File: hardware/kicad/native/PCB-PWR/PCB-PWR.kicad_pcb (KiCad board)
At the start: 4 copper layers, 90 x 60 mm, 66 parts, among them J1 43045-0213, J2 43045-1202, Q1 CSD18540Q5B, U1 LM74700QDBVRQ1, U2 INA226AIDGSR, U3 LMR604403SRAKR, U4 LMR604403SRAKR, U5 TPS7A2018PDBVR

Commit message: pcb-pwr: apply bootstrap routing candidate
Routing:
- net BOOT_3V8: track 0.00 -> 1.28 mm
- net BOOT_3V3: track 0.00 -> 1.28 mm
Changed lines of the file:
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@@
 		(layer "Edge.Cuts")
+	)
+	(segment
+		(start 54.925 15.125)
+		(end 55.055 16.4)
+		(width 0.5)
+		(layer "F.Cu")
+		(net 5)
+	)
+	(segment
+		(start 54.925 43.125)
+		(end 55.055 44.4)
+		(width 0.5)
+		(layer "F.Cu")
+		(net 4)
 	)
 	(embedded_fonts no)

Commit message: pcb-pwr: apply LM74700 VCAP routing candidate
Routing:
- net LM74700_VCAP: track 0.00 -> 3.16 mm
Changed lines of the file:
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@@
 		(net 4)
+	)
+	(segment
+		(start 18.7 29.05)
+		(end 19.52 26)
+		(width 0.5)
+		(layer "F.Cu")
+		(net 16)
 	)
 	(embedded_fonts no)

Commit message: pcb-pwr: apply VBAT_RAW routing candidate
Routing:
- net VBAT_RAW: track 0.00 -> 2.90 mm
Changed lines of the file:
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@@
 		(net 16)
+	)
+	(segment
+		(start 7.7 31.25)
+		(end 10.6 31.25)
+		(width 4)
+		(layer "F.Cu")
+		(net 30)
 	)
 	(embedded_fonts no)

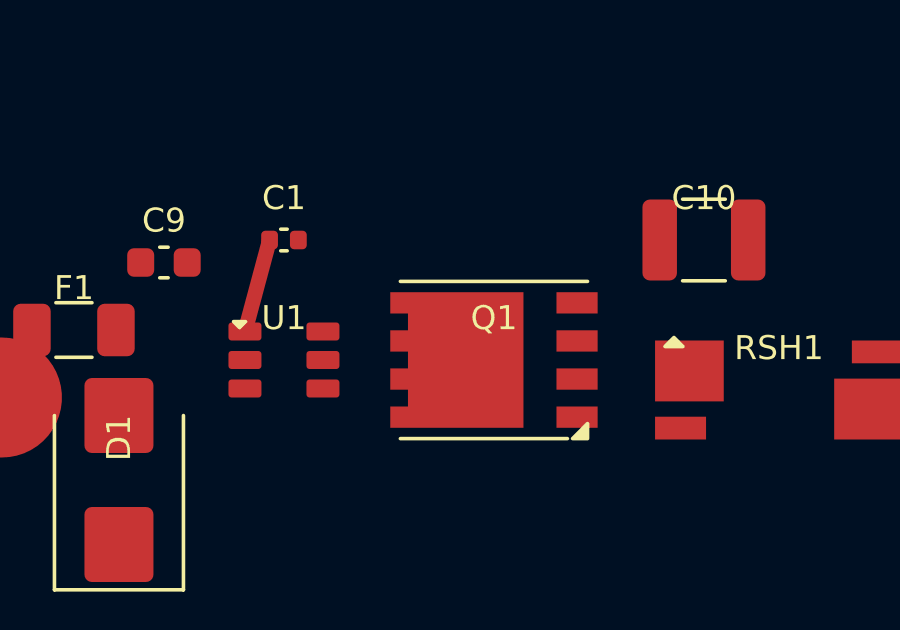
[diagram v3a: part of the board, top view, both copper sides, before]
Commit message: pcb-pwr: apply accepted REV_GATE route
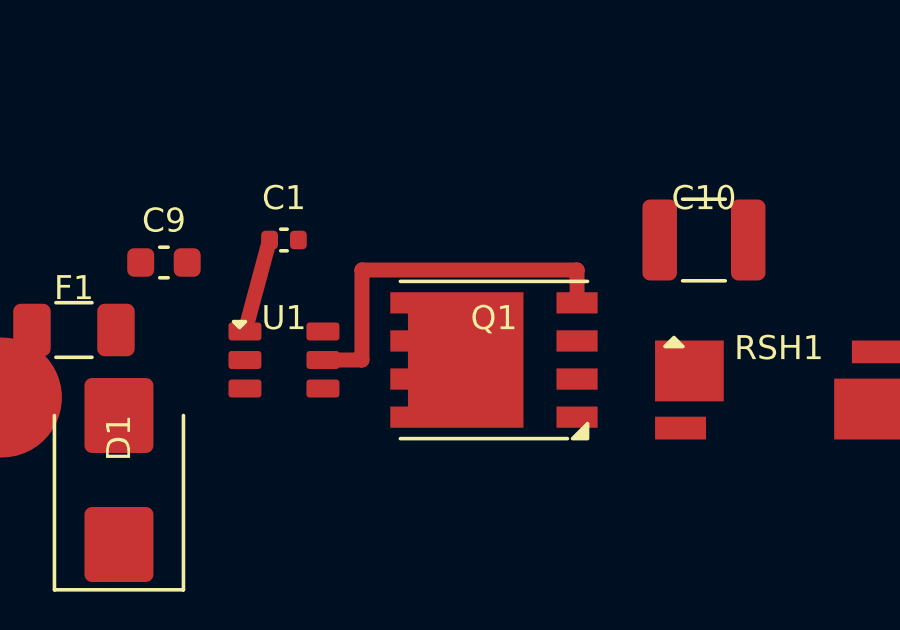
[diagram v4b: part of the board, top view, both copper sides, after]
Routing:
- net REV_GATE: track 0.00 -> 12.6 mm
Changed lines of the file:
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@@
 		(net 30)
+	)
+	(segment
+		(start 21.3 30)
+		(end 22.6 30)
+		(width 0.5)
+		(layer "F.Cu")
+		(net 21)
+	)
+	(segment
+		(start 22.6 30)
+		(end 22.6 27)
+		(width 0.5)
+		(layer "F.Cu")
+		(net 21)
+	)
+	(segment
+		(start 22.6 27)
+		(end 29.77 27)
+		(width 0.5)
+		(layer "F.Cu")
+		(net 21)
+	)
+	(segment
+		(start 29.77 27)
+		(end 29.77 28.095)
+		(width 0.5)
+		(layer "F.Cu")
+		(net 21)
 	)
 	(embedded_fonts no)

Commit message: hardware: apply PCB-PWR power-stage ECO-002
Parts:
- moved C4 4.00 mm to (57.8, 14.0), turned to 270 degrees
- moved C6 4.00 mm to (57.8, 42.0), turned to 270 degrees
- moved L1 1.75 mm to (62.5, 14.0)
- moved L2 1.75 mm to (62.5, 42.0)
- turned U3 to 90 degrees
- turned U4 to 90 degrees
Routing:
- net SW_3V8: track 0.00 -> 2.65 mm
- net SW_3V3: track 0.00 -> 2.65 mm

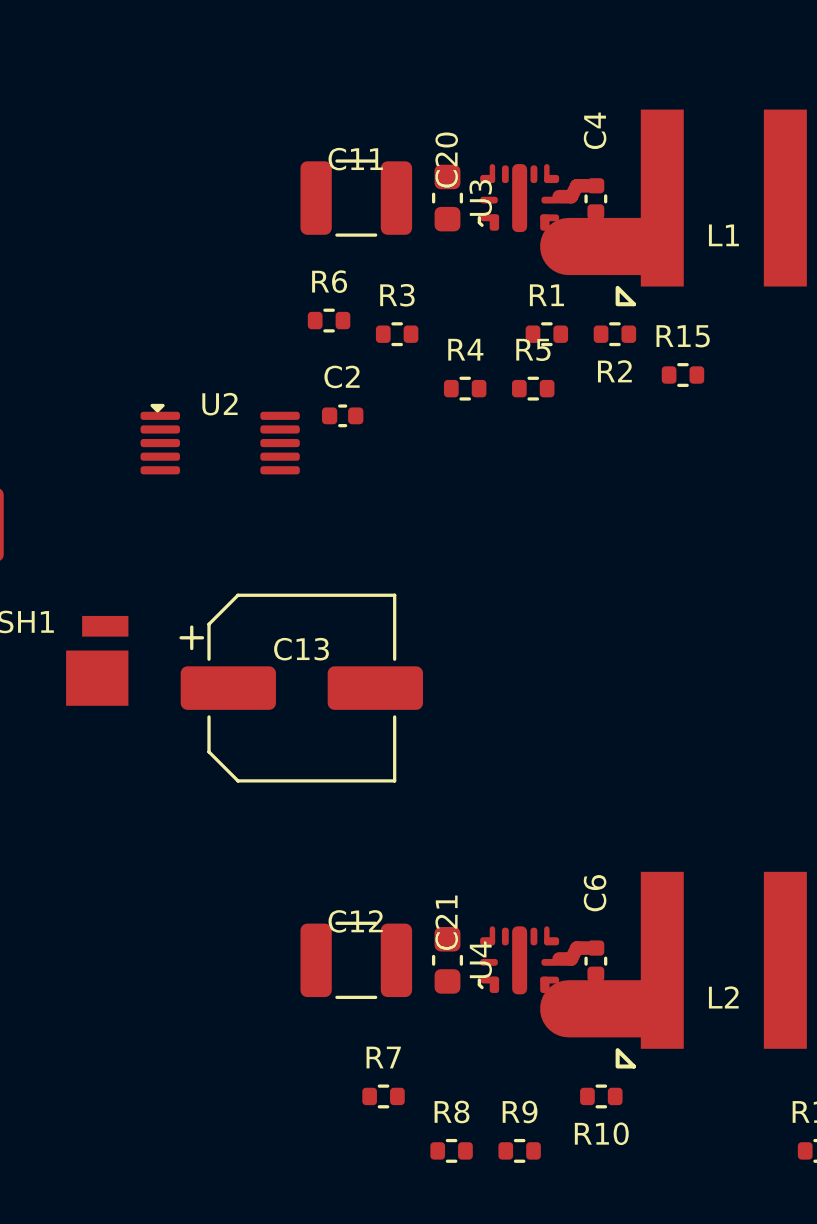
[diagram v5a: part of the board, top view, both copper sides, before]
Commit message: pcb-pwr: apply accepted buck input hot-loop routing 006 with audited gate
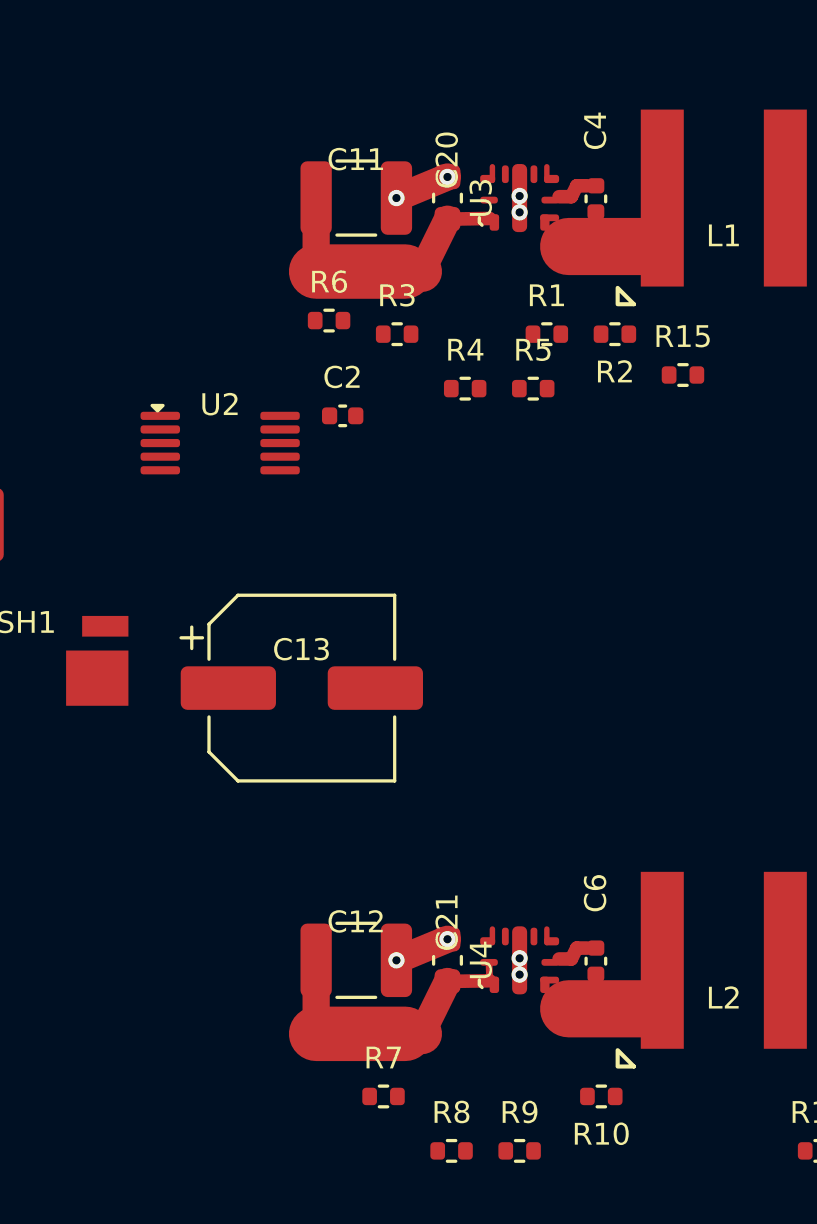
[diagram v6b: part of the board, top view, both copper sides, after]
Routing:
- net VBAT_SYS: track 0.00 -> 21.2 mm
- net GND_PWR: track 0.00 -> 4.06 mm, vias 0 -> 8
- added copper zone on In1.Cu, net GND_PWR
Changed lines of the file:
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@@
 		(net 26)
+	)
+	(segment
+		(start 47.525 14)
+		(end 47.525 16.7)
+		(width 1)
+		(layer "F.Cu")
+		(net 31)
+	)
+	(segment
+		(start 47.525 16.7)
+		(end 50.8 16.7)
+		(width 2)
+		(layer "F.Cu")
+		(net 31)
+	)
+	(segment
+		(start 50.8 16.7)
+		(end 51.4 16.7)
+		(width 1.5)
+		(layer "F.Cu")
+		(net 31)
+	)
+	(segment
+		(start 51.4 16.7)
+		(end 52.35 14.775)
+		(width 1)
+		(layer "F.Cu")
+		(net 31)
+	)
+	(segment
+		(start 52.35 14.775)
+		(end 53.9 14.75)
+		(width 0.5)
+		(layer "F.Cu")
+		(net 31)
+	)
+	(segment
+		(start 50.475 14)
+		(end 52.35 13.225)
+		(width 1)
+		(layer "F.Cu")
+		(net 13)
+	)
+	(segment
+		(start 47.525 42)
+		(end 47.525 44.7)
+		(width 1)
+		(layer "F.Cu")
+		(net 31)
+	)
+	(segment
+		(start 47.525 44.7)
+		(end 50.8 44.7)
+		(width 2)
+		(layer "F.Cu")
+		(net 31)
+	)
+	(segment
+		(start 50.8 44.7)
+		(end 51.4 44.7)
+		(width 1.5)
+		(layer "F.Cu")
+		(net 31)
+	)
+	(segment
+		(start 51.4 44.7)
+		(end 52.35 42.775)
+		(width 1)
+		(layer "F.Cu")
+		(net 31)
+	)
+	(segment
+		(start 52.35 42.775)
+		(end 53.9 42.75)
+		(width 0.5)
+		(layer "F.Cu")
+		(net 31)
+	)
+	(segment
+		(start 50.475 42)
+		(end 52.35 41.225)
+		(width 1)
+		(layer "F.Cu")
+		(net 13)
+	)
+	(segment
+		(start 53.9 42.75)
+		(end 53.875 42.075)
+		(width 0.25)
+		(layer "F.Cu")
+		(net 31)
+	)
+	(via
+		(at 50.475 14)
+		(size 0.6)
+		(drill 0.3)
+		(layers "F.Cu" "B.Cu")
+		(net 13)
+	)
+	(via
+		(at 52.35 13.225)
+		(size 0.6)
+		(drill 0.3)
+		(layers "F.Cu" "B.Cu")
+		(net 13)
+	)
+	(via
+		(at 55 13.925)
+		(size 0.6)
+		(drill 0.3)
+		(layers "F.Cu" "B.Cu")
+		(net 13)
+	)
+	(via
+		(at 55 14.525)
+		(size 0.6)
+		(drill 0.3)
+		(layers "F.Cu" "B.Cu")
+		(net 13)
+	)
+	(via
+		(at 50.475 42)
+		(size 0.6)
+		(drill 0.3)
+		(layers "F.Cu" "B.Cu")
+		(net 13)
+	)
+	(via
+		(at 52.35 41.225)
+		(size 0.6)
+		(drill 0.3)
+		(layers "F.Cu" "B.Cu")
+		(net 13)
+	)
+	(via
+		(at 55 41.925)
+		(size 0.6)
+		(drill 0.3)
+		(layers "F.Cu" "B.Cu")
+		(net 13)
+	)
+	(via
+		(at 55 42.525)
+		(size 0.6)
+		(drill 0.3)
+		(layers "F.Cu" "B.Cu")
+		(net 13)
+	)
+	(zone
+		(net 13)
+		(net_name "GND_PWR")
+		(layer "In1.Cu")
+		(name "PCB_PWR_3V8_LOCAL_HOT_LOOP_RETURN_In1_Cu")
+		(hatch edge 0.5)
+		(connect_pads yes
+			(clearance 0.3)
+		)
+		(min_thickness 0.25)
+		(fill yes
+			(thermal_gap 0.3)
+			(thermal_bridge_width 0.4)
+		)
+		(polygon
+			(pts
+				(xy 49.8 12.4)
+				(xy 55.35 12.4)
+				(xy 55.35 15.6)
+				(xy 49.8 15.6)
+			)
+		)
+	)
+	(zone
+		(net 13)
+		(net_name "GND_PWR")
+		(layer "In1.Cu")
+		(name "PCB_PWR_3V3_LOCAL_HOT_LOOP_RETURN_In1_Cu")
+		(hatch edge 0.5)
+		(connect_pads yes
+			(clearance 0.3)
+		)
+		(min_thickness 0.25)
+		(fill yes
+			(thermal_gap 0.3)
+			(thermal_bridge_width 0.4)
+		)
+		(polygon
+			(pts
+				(xy 49.8 40.4)
+				(xy 55.35 40.4)
+				(xy 55.35 43.6)
+				(xy 49.8 43.6)
+			)
+		)
 	)
 	(embedded_fonts no)

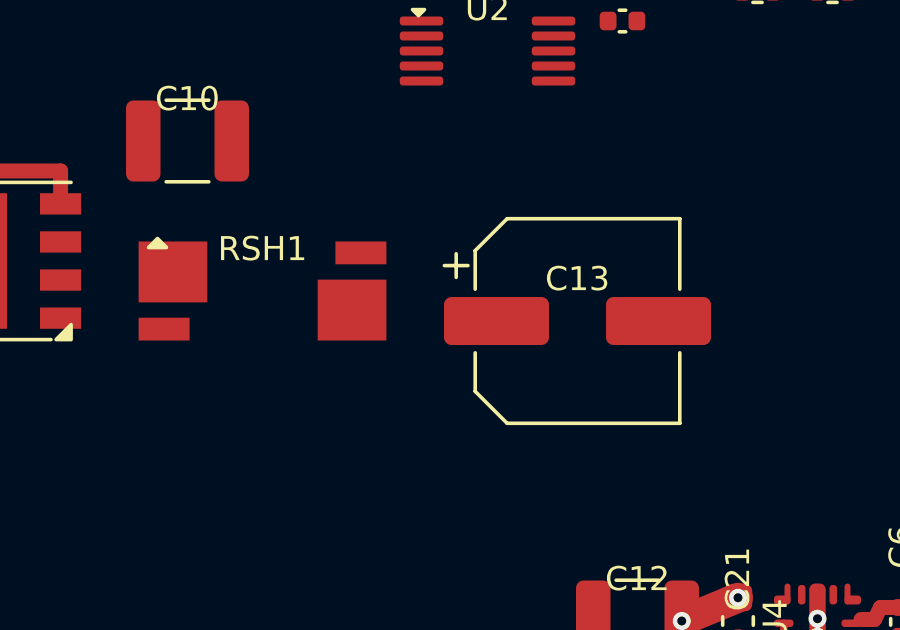
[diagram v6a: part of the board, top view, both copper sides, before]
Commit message: pcb-pwr: apply accepted shunt-to-bulk routing 007 with audited gate
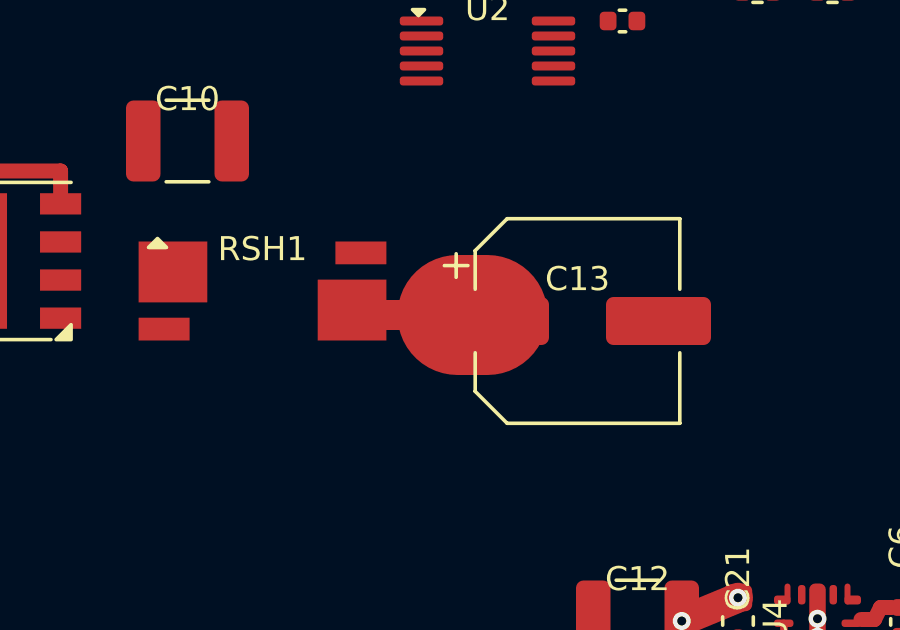
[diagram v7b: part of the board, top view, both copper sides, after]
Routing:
- net VBAT_SYS: track 21.2 -> 25.2 mm
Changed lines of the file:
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@@
 		)
+	)
+	(segment
+		(start 40 31.8)
+		(end 43 31.8)
+		(width 1)
+		(layer "F.Cu")
+		(net 31)
+	)
+	(segment
+		(start 43 31.8)
+		(end 44 31.8)
+		(width 4)
+		(layer "F.Cu")
+		(net 31)
 	)
 	(embedded_fonts no)

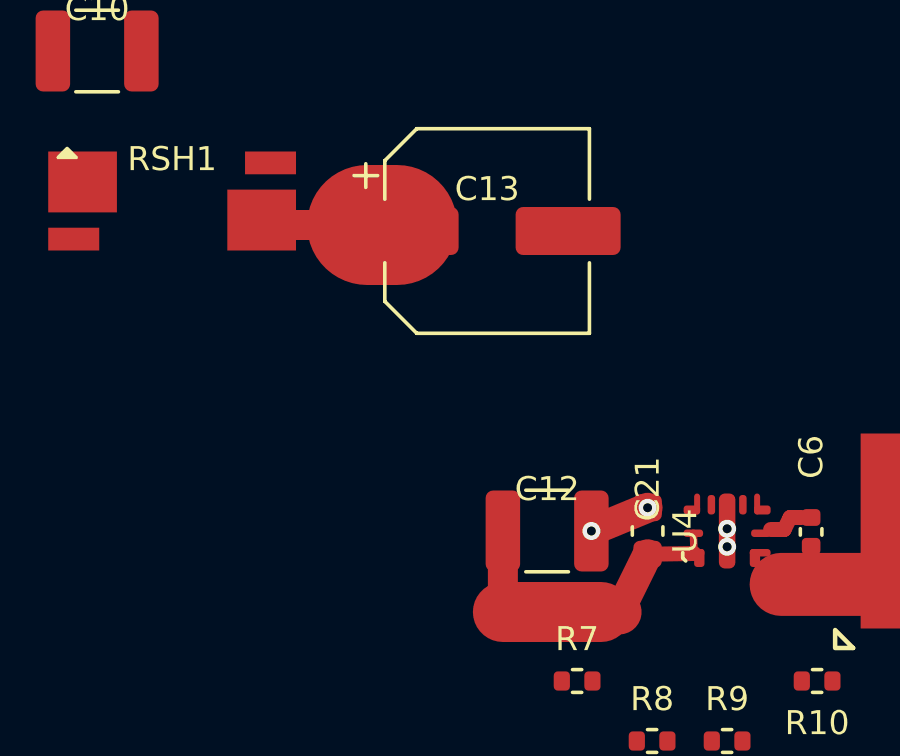
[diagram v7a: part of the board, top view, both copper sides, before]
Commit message: pcb-pwr: apply accepted C13-to-C12 routing 008 with audited gate
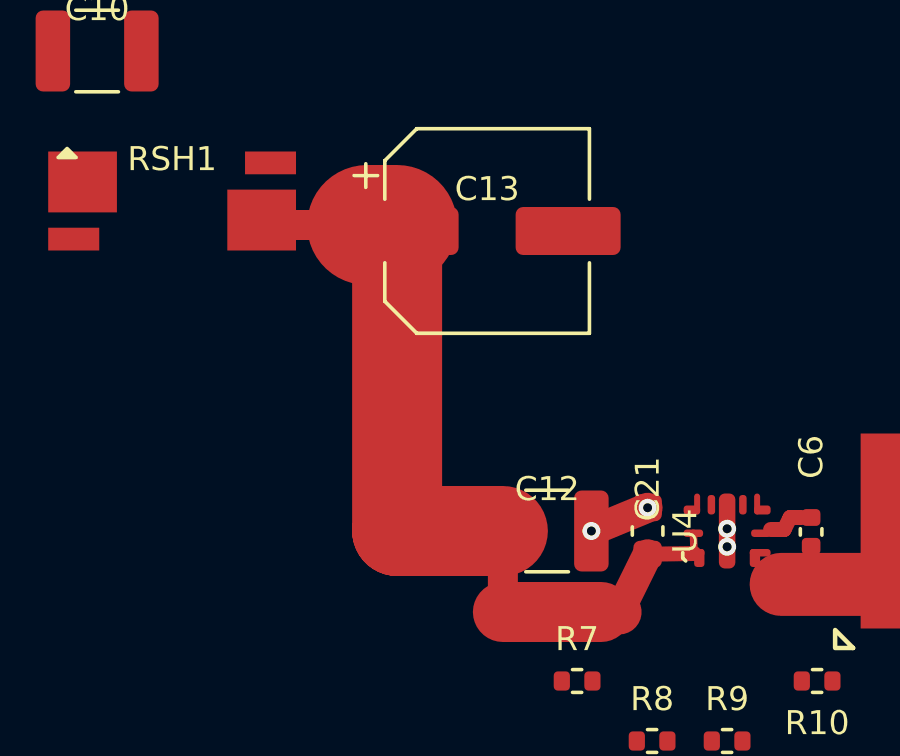
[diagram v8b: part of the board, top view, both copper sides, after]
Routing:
- net VBAT_SYS: track 25.2 -> 38.9 mm
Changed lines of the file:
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@@
+		(net 31)
+	)
+	(segment
+		(start 44 31.8)
+		(end 44 42)
+		(width 3)
+		(layer "F.Cu")
+		(net 31)
+	)
+	(segment
+		(start 44 42)
+		(end 47.525 42)
+		(width 3)
+		(layer "F.Cu")
 		(net 31)
 	)
